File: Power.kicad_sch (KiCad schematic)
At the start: 87 parts, among them U1 TPS546D24ARVFR, U3 TPSM861253RDXR, U4 TPS546D24ARVFR, U5 L78L05_SOT89

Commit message: add LCSC code
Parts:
- C1, C22: LCSC (none) -> C122327
- C10, C11, C12, C13, C14, C30, C31, C32, C33, C34, C35, C9: LCSC (none) -> C15008
- C15, C19, C36, C42, C46, C47: LCSC (none) -> C92827
- C16, C37: LCSC (none) -> C335105
- C17, C28, C7: LCSC (none) -> C5137487
- C18: LCSC (none) -> C277520
- C2, C23, C24, C3, C39, C43, C44: LCSC (none) -> C344022
- C20, C45: LCSC (none) -> C526997
- C29, C8: LCSC (none) -> C46653
- R1, R8: LCSC (none) -> C87044
- R11, R7: LCSC (none) -> C138055
- R13: LCSC (none) -> C183355
- R15, R2: LCSC (none) -> C253344
- R16, R3: LCSC (none) -> C138066
- R17: LCSC (none) -> C93942
- R18, R19, R5, R6: LCSC (none) -> C60489
- R21, R22, R40: LCSC (none) -> C105870
- R37, R38, R39: LCSC (none) -> C60485
- R4: LCSC (none) -> C137935
- U1, U4: LCSC (none) -> C507280
- U5: LCSC (none) -> C353038

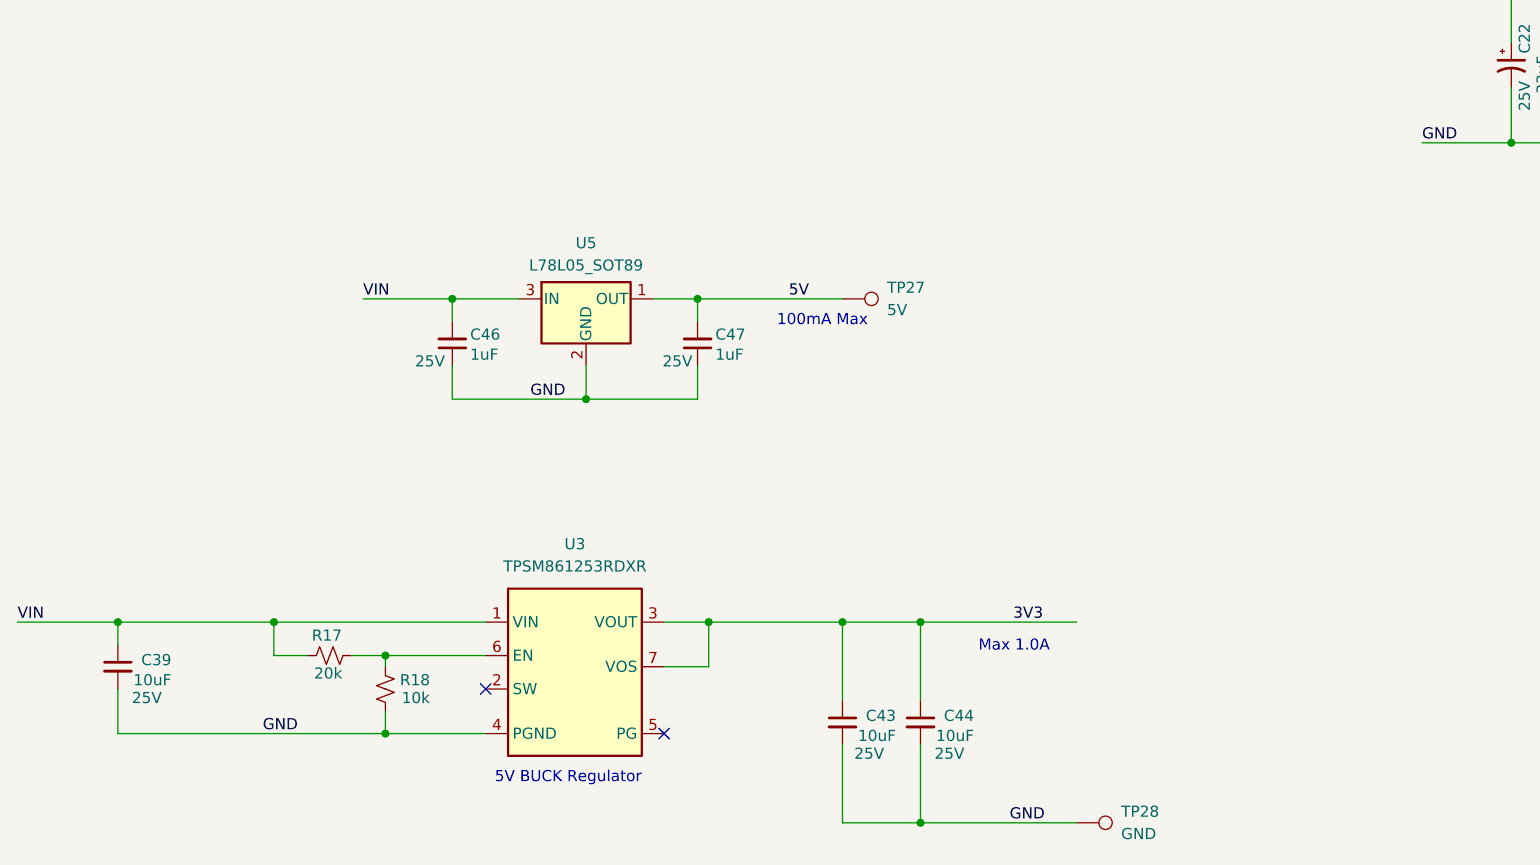
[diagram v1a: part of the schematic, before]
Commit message: Start changing ldo to match our production
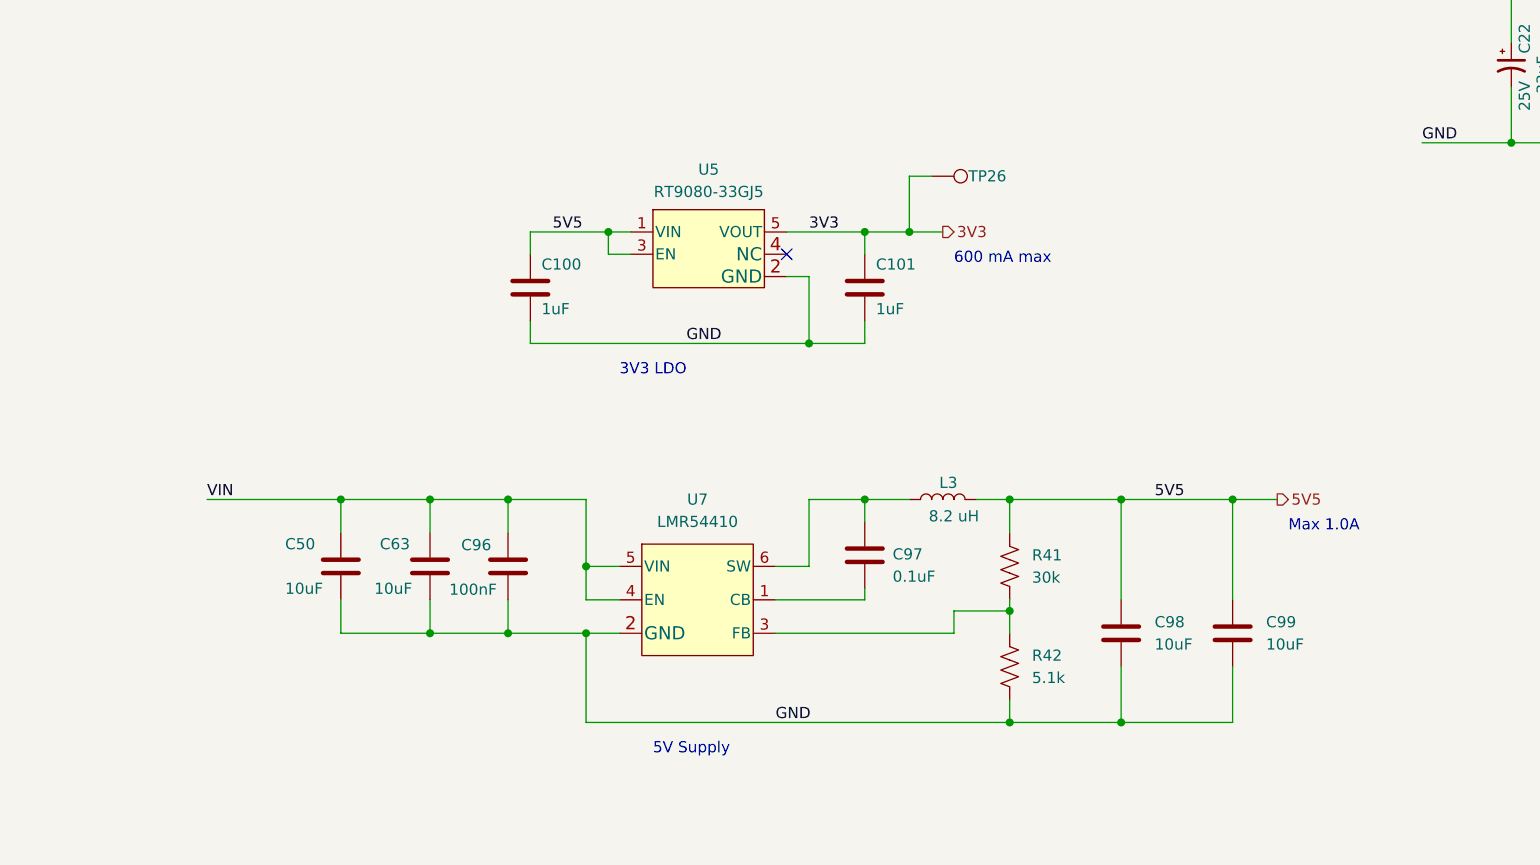
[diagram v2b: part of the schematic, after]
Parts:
- removed C39, C43, C44: 10uF, Capacitor_SMD:C_0603_1608Metric, symbol Device:C_Small
- removed C46, C47: 1uF, Capacitor_SMD:C_0402_1005Metric, symbol Device:C_Small
- removed R17: 20k, Resistor_SMD:R_0402_1005Metric, symbol Device:R_Small_US
- removed R18: 10k, Resistor_SMD:R_0402_1005Metric, symbol Device:R_Small_US
- removed TP27: 5V, TestPoint:TestPoint_Pad_D1.5mm, symbol Connector:TestPoint
- removed TP28: GND, TestPoint:TestPoint_Pad_D1.5mm, symbol Connector:TestPoint
- removed U3: TPSM861253RDXR, bitaxe:TPSM863257RDX, symbol bitaxe:TPSM861253RDXR
- removed U5: L78L05_SOT89, Package_TO_SOT_SMD:SOT-89-3, symbol Regulator_Linear:L78L05_SOT89
- added C100, C101: 1uF, Capacitor_SMD:C_0402_1005Metric, symbol Device:C
- added C50, C63, C98, C99: 10uF, Capacitor_SMD:C_0805_2012Metric, symbol Device:C
- added C96: 100nF, Capacitor_SMD:C_0603_1608Metric, symbol Device:C
- added C97: 0.1uF, Capacitor_SMD:C_0402_1005Metric, symbol Device:C
- added L3: 8.2 uH, Zyber:74438357082, symbol Device:L
- added R41: 30k, Resistor_SMD:R_0402_1005Metric, symbol Device:R_US
- added R42: 5.1k, Resistor_SMD:R_0402_1005Metric, symbol Device:R_US
- added TP26: TestPoint, TestPoint:TestPoint_Pad_D1.0mm, symbol Connector:TestPoint
- added U5: RT9080-33GJ5, Zyber:RT9080-33GJ5, symbol bitaxe:RT9080-33GJ5
- added U7: LMR54410, Package_TO_SOT_SMD:SOT-23-6, symbol bitaxe:LMR54410
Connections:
- net 12V: now also C50.1, C63.1, C96.2, U7.4 (EN), U7.5 (VIN)
- net 3V3: now also C101.1, TP26.1, U5.5 (VOUT)
- net GND: now also C100.2, C101.2, C50.2, C63.2, C96.1, C98.2, C99.2, R42.2, U5.2 (GND), U7.2 (GND)
- new net: C97.1, L3.1, U7.6 (SW)
- new net: C97.2, U7.1 (CB)
- new net: R41.2, R42.1, U7.3 (FB)
- new net 5V5: C100.1, C98.1, C99.1, L3.2, R41.1, U5.1 (VIN), U5.3 (EN)
- no-connect marks 6 -> 5
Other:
- note added: "3V3 LDO"
- note added: "5V Supply"
- note added: "600 mA max"
- note removed: "100mA Max"
- note removed: "5V BUCK Regulator"

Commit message: final update
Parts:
- removed TP26: TestPoint, TestPoint:TestPoint_Pad_D1.0mm, symbol Connector:TestPoint
- C100, C101: LCSC (none) -> C181017
- C50, C63, C98, C99: LCSC (none) -> C2190942
- C96: LCSC (none) -> C14663
- C97: LCSC (none) -> C5137487
- L1, L2: value 300nH -> 220nH; DK (none) -> YLSI100808-R22K; LCSC (none) -> C20613221; PARTNO SLC1175-271MEC -> YLSI100808-R22K
- L3: LCSC (none) -> C9900143873
- R41: LCSC (none) -> C412503
- R42: LCSC (none) -> C105872
- U5: LCSC (none) -> C841192
- U7: LCSC (none) -> C3193115
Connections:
- net 5V5 is gone; now on net 5V: C100.1, C98.1, C99.1, L3.2, R41.1, U5.1 (VIN), U5.3 (EN)
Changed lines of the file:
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@@
 	)
 	(junction
-		(at 124.46 180.34)
-		(diameter 0)
-		(color 0 0 0 0)
-	)
-	(junction
 		(at 181.61 105.41)
 		(diameter 0)
@@
 	(wire
 		(pts
-			(xy 124.46 180.34) (xy 128.27 180.34)
+			(xy 119.38 180.34) (xy 128.27 180.34)
 		)
 		(stroke
@@
 	(wire
 		(pts
-			(xy 127 173.99) (xy 124.46 173.99)
-		)
-		(stroke
-			(width 0)
-			(type default)
-		)
-	)
-	(wire
-		(pts
 			(xy 200.66 163.83) (xy 200.66 170.18)
 		)
@@
 	(wire
 		(pts
-			(xy 124.46 173.99) (xy 124.46 180.34)
-		)
-		(stroke
-			(width 0)
-			(type default)
-		)
-	)
-	(wire
-		(pts
 			(xy 237.49 66.04) (xy 241.3 66.04)
 		)
@@
 	(wire
 		(pts
-			(xy 119.38 180.34) (xy 124.46 180.34)
-		)
-		(stroke
-			(width 0)
-			(type default)
-		)
-	)
-	(wire
-		(pts
 			(xy 269.24 168.91) (xy 271.78 168.91)
 		)
@@
 		)
 	)
-	(label "5V5"
+	(label "5V"
 		(at 152.4 210.82 0)
 		(effects
@@
 		)
 	)
-	(label "5V5"
+	(label "5V"
 		(at 83.82 180.34 0)
 		(effects
@@
 		)
 	)
-	(hierarchical_label "5V5"
+	(hierarchical_label "5V"
 		(shape output)
 		(at 166.37 210.82 0)
@@
 			)
 		)
+		(property "LCSC" "C14663"
+			(at 78.74 218.44 0)
+			(effects
+				(font
+					(size 1.27 1.27)
+				)
+			)
+		)
 		(pin "1"
 		)
@@
 			)
 		)
+		(property "LCSC" "C2190942"
+			(at 161.29 226.06 0)
+			(effects
+				(font
+					(size 1.27 1.27)
+				)
+			)
+		)
 		(pin "1"
 		)
@@
 			)
 		)
+		(property "LCSC" "C5137487"
+			(at 119.38 217.17 0)
+			(effects
+				(font
+					(size 1.27 1.27)
+				)
+			)
+		)
 		(pin "1"
 		)
@@
 			)
 		)
+		(property "LCSC" "C2190942"
+			(at 148.59 226.06 0)
+			(effects
+				(font
+					(size 1.27 1.27)
+				)
+			)
+		)
 		(pin "1"
 		)
@@
 			)
 		)
+		(property "LCSC" "C181017"
+			(at 81.28 186.69 0)
+			(effects
+				(font
+					(size 1.27 1.27)
+				)
+			)
+		)
 		(pin "1"
 		)
@@
 			)
 		)
-		(property "Value" "300nH"
+		(property "Value" "220nH"
 			(at 297.18 52.07 90)
 			(effects
@@
 			)
 		)
-		(property "PARTNO" "SLC1175-271MEC"
+		(property "PARTNO" "YLSI100808-R22K"
 			(at 297.18 54.61 90)
 			(effects
@@
 			)
 		)
-		(property "DK" ""
+		(property "DK" "YLSI100808-R22K"
 			(at 297.18 54.61 0)
 			(effects
@@
 			)
 		)
+		(property "LCSC" "C20613221"
+			(at 297.18 54.61 0)
+			(effects
+				(font
+					(size 1.27 1.27)
+				)
+			)
+		)
 		(pin "1"
 		)
@@
 			)
 		)
+		(property "LCSC" "C841192"
+			(at 101.6 181.61 0)
+			(effects
+				(font
+					(size 1.27 1.27)
+				)
+			)
+		)
 		(pin "1"
 		)
@@
 			)
 		)
+		(property "LCSC" "C3193115"
+			(at 100.33 222.25 0)
+			(effects
+				(font
+					(size 1.27 1.27)
+				)
+			)
+		)
 		(pin "1"
 		)
@@
 	)
 	(symbol
-		(lib_id "Connector:TestPoint")
-		(at 127 173.99 270)
-		(mirror x)
-		(unit 1)
-		(exclude_from_sim no)
-		(in_bom no)
-		(on_board yes)
-		(dnp no)
-		(property "Reference" "TP26"
-			(at 133.35 173.99 90)
-			(effects
-				(font
-					(size 1.27 1.27)
-				)
-			)
-		)
-		(property "Value" "TestPoint"
-			(at 132.715 172.7201 90)
-			(effects
-				(font
-					(size 1.27 1.27)
-				)
-				(justify left)
-				(hide yes)
-			)
-		)
-		(property "Footprint" "TestPoint:TestPoint_Pad_D1.0mm"
-			(at 127 168.91 0)
-			(effects
-				(font
-					(size 1.27 1.27)
-				)
-				(hide yes)
-			)
-		)
-		(property "Datasheet" "~"
-			(at 127 168.91 0)
-			(effects
-				(font
-					(size 1.27 1.27)
-				)
-				(hide yes)
-			)
-		)
-		(property "Description" ""
-			(at 127 173.99 0)
-			(effects
-				(font
-					(size 1.27 1.27)
-				)
-				(hide yes)
-			)
-		)
-		(property "嘉立创元件编号" ""
-			(at 127 173.99 0)
-			(effects
-				(font
-					(size 1.27 1.27)
-				)
-				(hide yes)
-			)
-		)
-		(pin "1"
-		)
-		(instances
-			(project "BitaxeGT"
-				(path "/61fe8d2c-9301-4ad9-8caf-c47acfa835b0/24036843-8461-4d4b-b738-f953c909ed6c"
-					(reference "TP26")
-					(unit 1)
-				)
-			)
-		)
-	)
-	(symbol
 		(lib_id "Device:R_Small_US")
 		(at 229.87 182.88 270)
@@
 			)
 		)
+		(property "LCSC" "C181017"
+			(at 119.38 186.69 0)
+			(effects
+				(font
+					(size 1.27 1.27)
+				)
+			)
+		)
 		(pin "1"
 		)
@@
 			)
 		)
+		(property "LCSC" "C9900143873"
+			(at 128.27 210.82 0)
+			(effects
+				(font
+					(size 1.27 1.27)
+				)
+			)
+		)
 		(pin "1"
 		)
@@
 			)
 		)
+		(property "LCSC" "C105872"
+			(at 135.89 229.87 0)
+			(effects
+				(font
+					(size 1.27 1.27)
+				)
+			)
+		)
 		(pin "1"
 		)
@@
 			)
 		)
+		(property "LCSC" "C412503"
+			(at 135.89 218.44 0)
+			(effects
+				(font
+					(size 1.27 1.27)
+				)
+			)
+		)
 		(pin "1"
 		)
@@
 			)
 		)
-		(property "Value" "300nH"
+		(property "Value" "220nH"
 			(at 298.45 166.37 90)
 			(effects
@@
 			)
 		)
-		(property "PARTNO" "SLC1175-271MEC"
+		(property "PARTNO" "YLSI100808-R22K"
 			(at 298.45 168.91 90)
 			(effects
@@
 			)
 		)
-		(property "DK" ""
+		(property "DK" "YLSI100808-R22K"
+			(at 298.45 168.91 0)
+			(effects
+				(font
+					(size 1.27 1.27)
+				)
+			)
+		)
+		(property "LCSC" "C20613221"
 			(at 298.45 168.91 0)
 			(effects
@@
 			)
 		)
+		(property "LCSC" "C2190942"
+			(at 69.85 218.44 0)
+			(effects
+				(font
+					(size 1.27 1.27)
+				)
+			)
+		)
 		(pin "1"
 		)
@@
 			)
 		)
+		(property "LCSC" "C2190942"
+			(at 59.69 218.44 0)
+			(effects
+				(font
+					(size 1.27 1.27)
+				)
+			)
+		)

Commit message: change cap
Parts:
- C15, C19, C36, C42: LCSC C92827 -> C77009
- C16, C37: LCSC C335105 -> C23733
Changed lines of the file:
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@@
 			)
 		)
-		(property "LCSC" "C92827"
+		(property "LCSC" "C77009"
 			(at 236.22 91.44 90)
 			(effects
@@
 			)
 		)
-		(property "LCSC" "C335105"
+		(property "LCSC" "C23733"
 			(at 212.09 195.58 90)
 			(effects
@@
 			)
 		)
-		(property "LCSC" "C92827"
+		(property "LCSC" "C77009"
 			(at 219.71 68.58 90)
 			(effects
@@
 			)
 		)
-		(property "LCSC" "C92827"
+		(property "LCSC" "C77009"
 			(at 219.71 182.88 90)
 			(effects
@@
 			)
 		)
-		(property "LCSC" "C335105"
+		(property "LCSC" "C23733"
 			(at 219.71 81.28 90)
 			(effects
@@
 			)
 		)
-		(property "LCSC" "C92827"
+		(property "LCSC" "C77009"
 			(at 236.22 205.74 90)
 			(effects
